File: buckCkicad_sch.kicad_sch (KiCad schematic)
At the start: 20 parts, among them U6 SiC437BED-T1-GE3

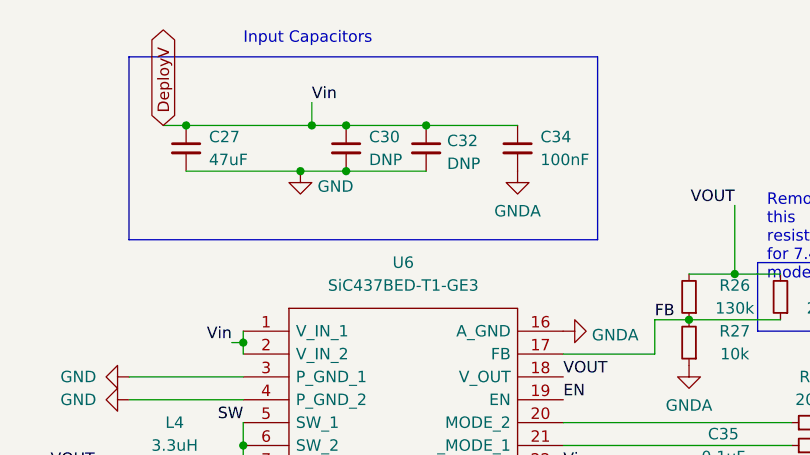
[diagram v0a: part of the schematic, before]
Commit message: added 30V input caps
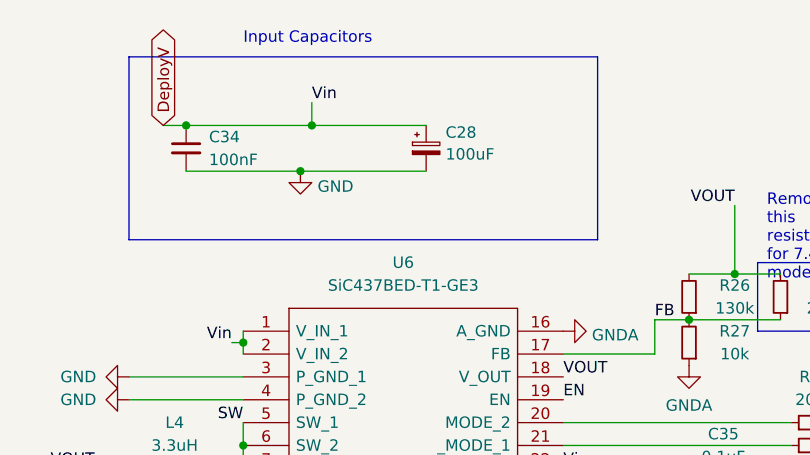
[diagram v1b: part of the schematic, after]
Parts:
- removed C27: 47uF, Capacitor_SMD:C_1206_3216Metric, symbol Device:C_Small
- removed C30, C32: DNP, Capacitor_SMD:C_1206_3216Metric, symbol Device:C_Small
- added C28: 100uF, Capacitor_Tantalum_SMD:CP_EIA-7343-40_Kemet-Y, symbol Device:C_Polarized_Small
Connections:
- net DeployV: now also C28.1
- net GND: now also C28.2
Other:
- moved on the sheet: C34

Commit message: Andrei review changes
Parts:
- C29: symbol Device:C_Small -> Device:C_Polarized
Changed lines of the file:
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@@
+	)
+	(junction
+		(at 92.456 115.57)
+		(diameter 0)
+		(color 0 0 0 0)
 	)
 	(junction
@@
 	(junction
 		(at 74.93 66.04)
-		(diameter 0)
-		(color 0 0 0 0)
-	)
-	(junction
-		(at 92.456 115.57)
 		(diameter 0)
 		(color 0 0 0 0)
@@
 	)
 	(symbol
-		(lib_id "Device:C_Small")
-		(at 92.456 118.11 0)
+		(lib_id "Device:C_Polarized")
+		(at 92.456 119.38 0)
 		(unit 1)
 		(exclude_from_sim no)
@@
 		(fields_autoplaced yes)
 		(property "Reference" "C29"
-			(at 95.25 116.8462 0)
+			(at 96.52 117.2209 0)
 			(effects
 				(font
@@
 		)
 		(property "Value" "470uF"
-			(at 95.25 119.3862 0)
+			(at 96.52 119.7609 0)
 			(effects
 				(font
@@
 		)
 		(property "Footprint" "Capacitor_SMD:CP_Elec_6.3x7.7"
-			(at 92.456 118.11 0)
+			(at 93.4212 123.19 0)
 			(effects
 				(font
@@
 		)
 		(property "Datasheet" "~"
-			(at 92.456 118.11 0)
-			(effects
-				(font
-					(size 1.27 1.27)
-				)
-				(hide yes)
-			)
-		)
-		(property "Description" ""
-			(at 92.456 118.11 0)
+			(at 92.456 119.38 0)
+			(effects
+				(font
+					(size 1.27 1.27)
+				)
+				(hide yes)
+			)
+		)
+		(property "Description" "Polarized capacitor"
+			(at 92.456 119.38 0)
 			(effects
 				(font
@@
 	(symbol
 		(lib_id "power:GND")
-		(at 92.456 120.65 0)
+		(at 92.456 123.19 0)
 		(unit 1)
 		(exclude_from_sim no)
@@
 		(fields_autoplaced yes)
 		(property "Reference" "#PWR065"
-			(at 92.456 127 0)
+			(at 92.456 129.54 0)
 			(effects
 				(font
@@
 		)
 		(property "Value" "GND"
-			(at 94.361 122.3538 0)
+			(at 94.361 124.8938 0)
 			(effects
 				(font
@@
 		)
 		(property "Footprint" ""
-			(at 92.456 120.65 0)
+			(at 92.456 123.19 0)
 			(effects
 				(font
@@
 		)
 		(property "Datasheet" ""
-			(at 92.456 120.65 0)
+			(at 92.456 123.19 0)
 			(effects
 				(font
@@
 		)
 		(property "Description" ""
-			(at 92.456 120.65 0)
-			(effects
-				(font
+			(at 92.456 123.19 0)
+			(effects
+				(font
